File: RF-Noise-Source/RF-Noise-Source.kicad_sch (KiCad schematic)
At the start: 44 parts

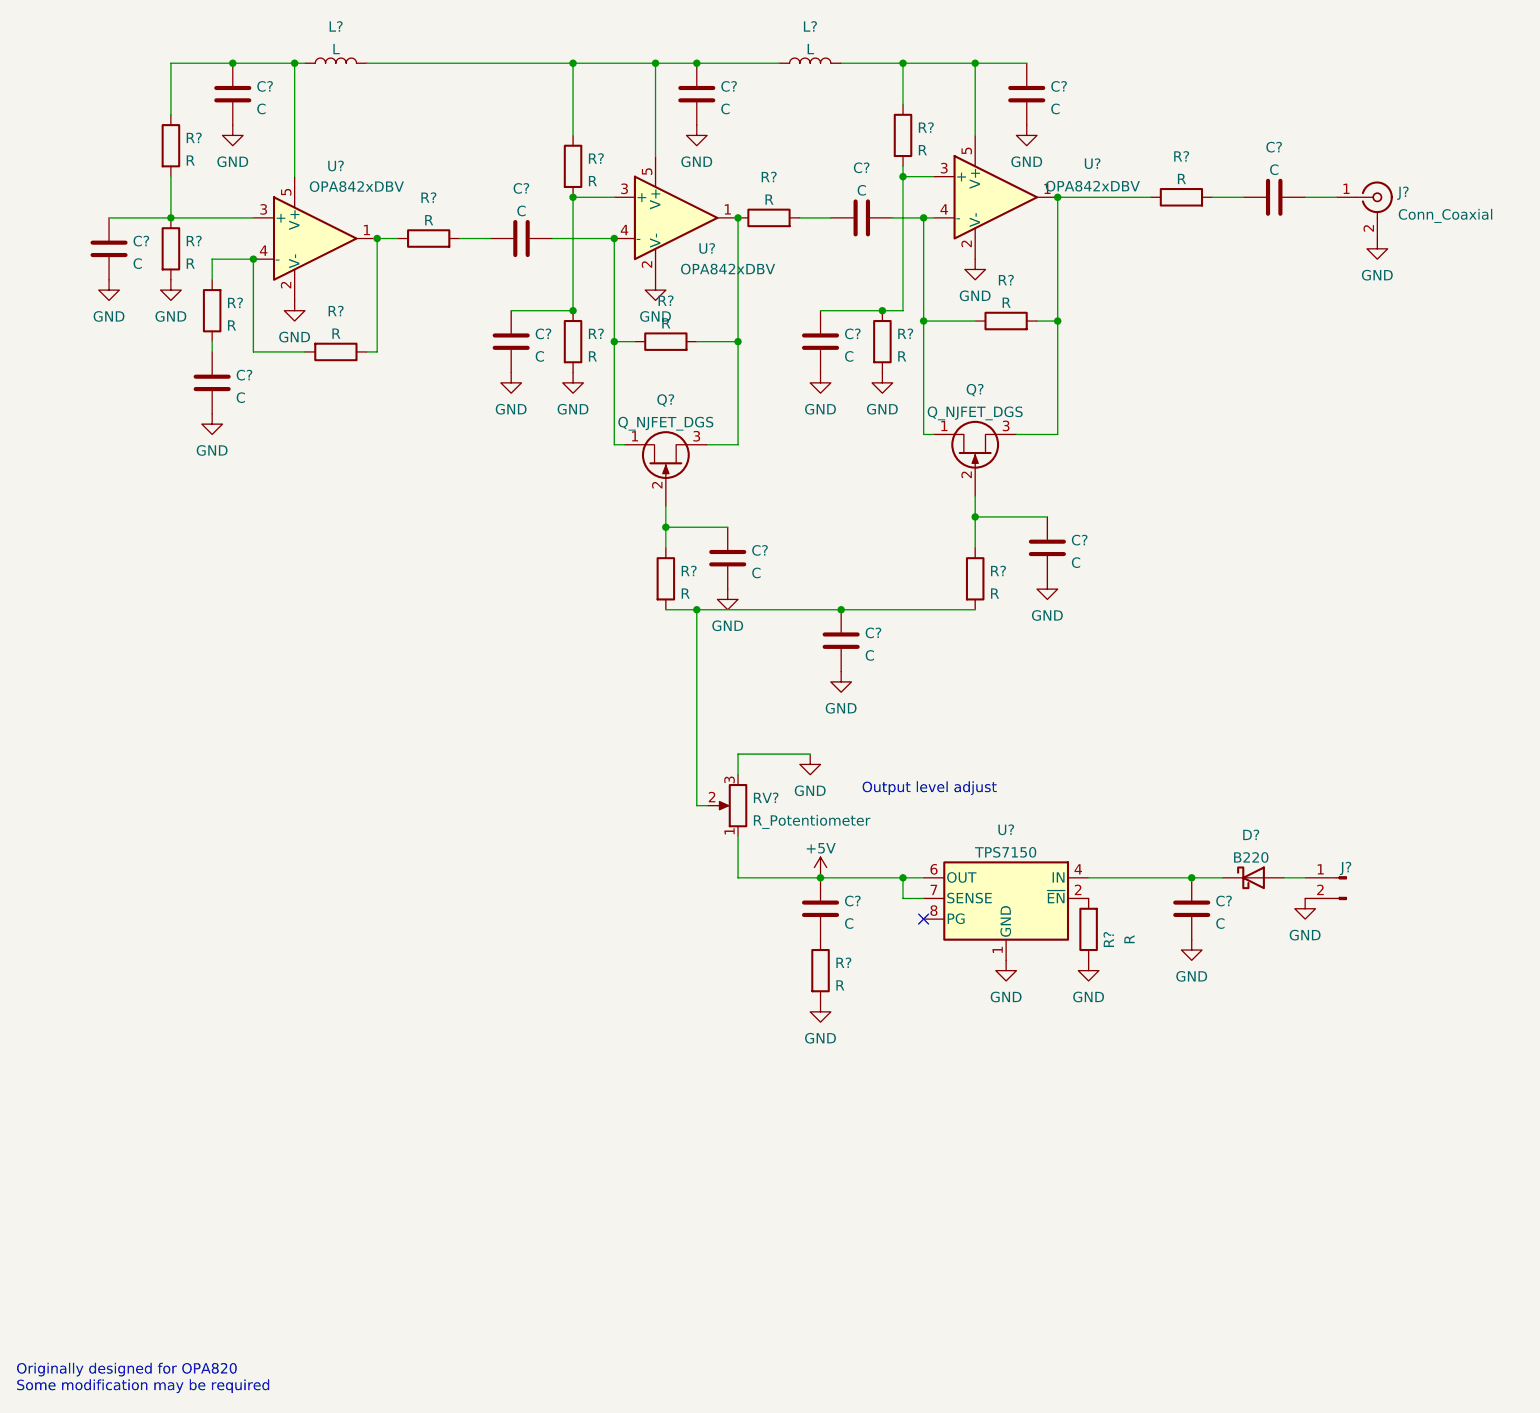
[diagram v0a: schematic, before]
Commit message: schematic capture completed, beginning PCB layout
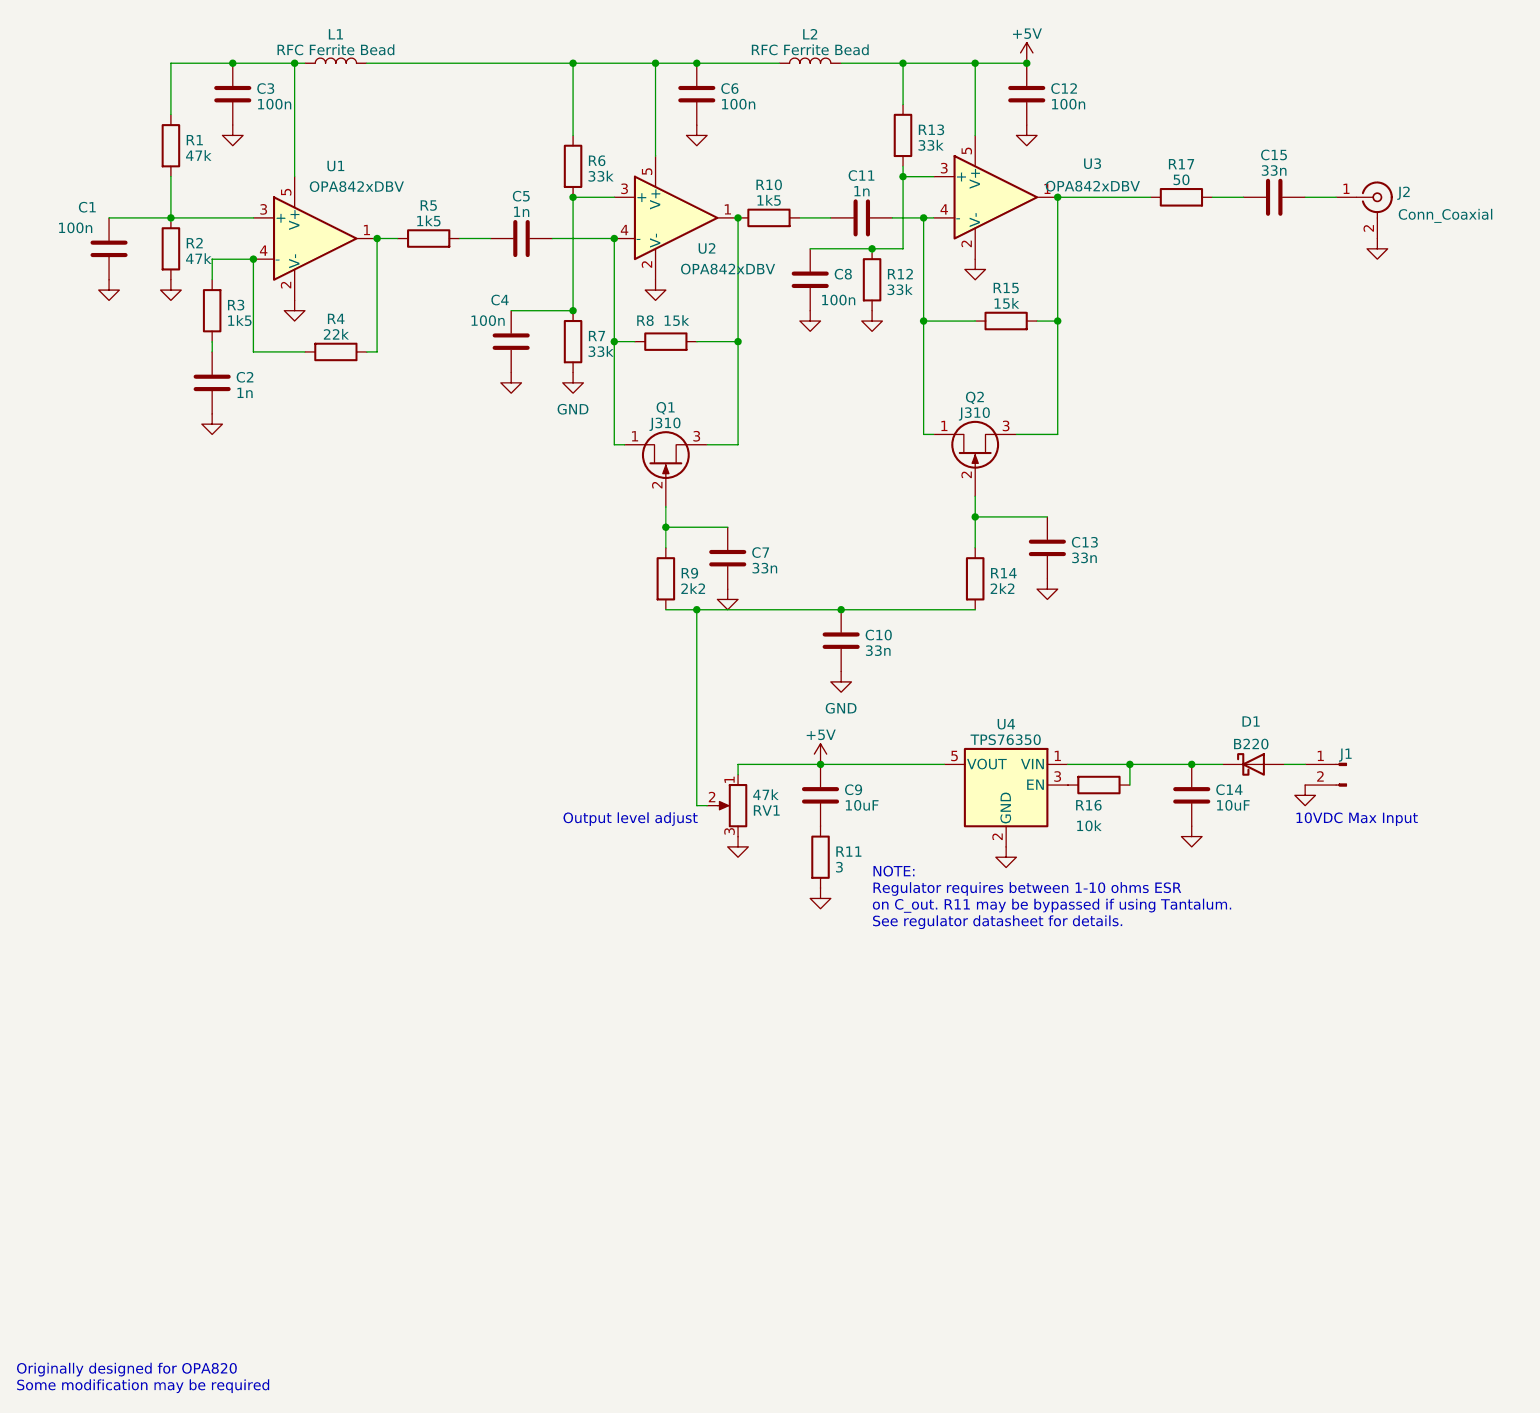
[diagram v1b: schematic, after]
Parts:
- removed U?: TPS7150, symbol Regulator_Linear:TPS7150
- added U4: TPS76350, Package_TO_SOT_SMD:SOT-23-5, symbol Regulator_Linear:TPS76350
- C1, C12, C3, C4, C6, C8: renamed from C?; value C -> 100n; footprint (none) -> Capacitor_SMD:C_0603_1608Metric
- C10, C13, C15, C7: renamed from C?; value C -> 33n; footprint (none) -> Capacitor_SMD:C_0603_1608Metric
- C11, C2, C5: renamed from C?; value C -> 1n; footprint (none) -> Capacitor_SMD:C_0603_1608Metric
- C14, C9: renamed from C?; value C -> 10uF; footprint (none) -> Capacitor_SMD:C_0603_1608Metric
- J1: renamed from J?; footprint (none) -> Connector_Molex:Molex_KK-254_AE-6410-02A_1x02_P2.54mm_Vertical
- J2: renamed from J?; footprint (none) -> Connector_Coaxial:SMA_Molex_73251-1153_EdgeMount_Horizontal
- L1, L2: renamed from L?; value L -> RFC Ferrite Bead; footprint (none) -> Inductor_SMD:L_0805_2012Metric
- Q1, Q2: renamed from Q?; value Q_NJFET_DGS -> J310; footprint (none) -> Package_TO_SOT_SMD:SOT-23
- R1, R2: renamed from R?; value R -> 47k; footprint (none) -> Resistor_SMD:R_0603_1608Metric
- R10, R3, R5: renamed from R?; value R -> 1k5; footprint (none) -> Resistor_SMD:R_0603_1608Metric
- R11: renamed from R?; value R -> 3; footprint (none) -> Resistor_SMD:R_0603_1608Metric
- R12, R13, R6, R7: renamed from R?; value R -> 33k; footprint (none) -> Resistor_SMD:R_0603_1608Metric
- R14, R9: renamed from R?; value R -> 2k2; footprint (none) -> Resistor_SMD:R_0603_1608Metric
- R15, R8: renamed from R?; value R -> 15k; footprint (none) -> Resistor_SMD:R_0603_1608Metric
- R16: renamed from R?; value R -> 10k; footprint (none) -> Resistor_SMD:R_0603_1608Metric
- R17: renamed from R?; value R -> 50; footprint (none) -> Resistor_SMD:R_0603_1608Metric
- R4: renamed from R?; value R -> 22k; footprint (none) -> Resistor_SMD:R_0603_1608Metric
- RV1: renamed from RV?; value R_Potentiometer -> 47k; footprint (none) -> Potentiometer_SMD:Potentiometer_Bourns_3214W_Vertical
- gave numbers to parts that had none: 4
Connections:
- net +5V: now also C12.1, L2.2, R13.1, U3.5 (V+), U4.5 (VOUT)
- net GND: now also U4.2 (GND); no longer R16.1
- net at C14.1, D1.1 (K): now also R16.1, U4.1 (VIN)
- net at R16.2: now also U4.3 (EN)
- no-connect marks 1 -> 0
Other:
- note added: "10VDC Max Input"
- note added: "NOTE: Regulator requires between 1-10 ohms ESR on C_out. R11 may be bypassed if using Tantalum. See regulator datasheet for details."
- moved on the sheet: C14, C8, C9, D1, J1, R11, R12, R16, RV1
